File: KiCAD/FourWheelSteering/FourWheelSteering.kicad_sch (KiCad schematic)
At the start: 11 parts, among them J1 Conn_01x04_Pin, U1 Q1, U2 Q3, U3 Q2, U4 Q4

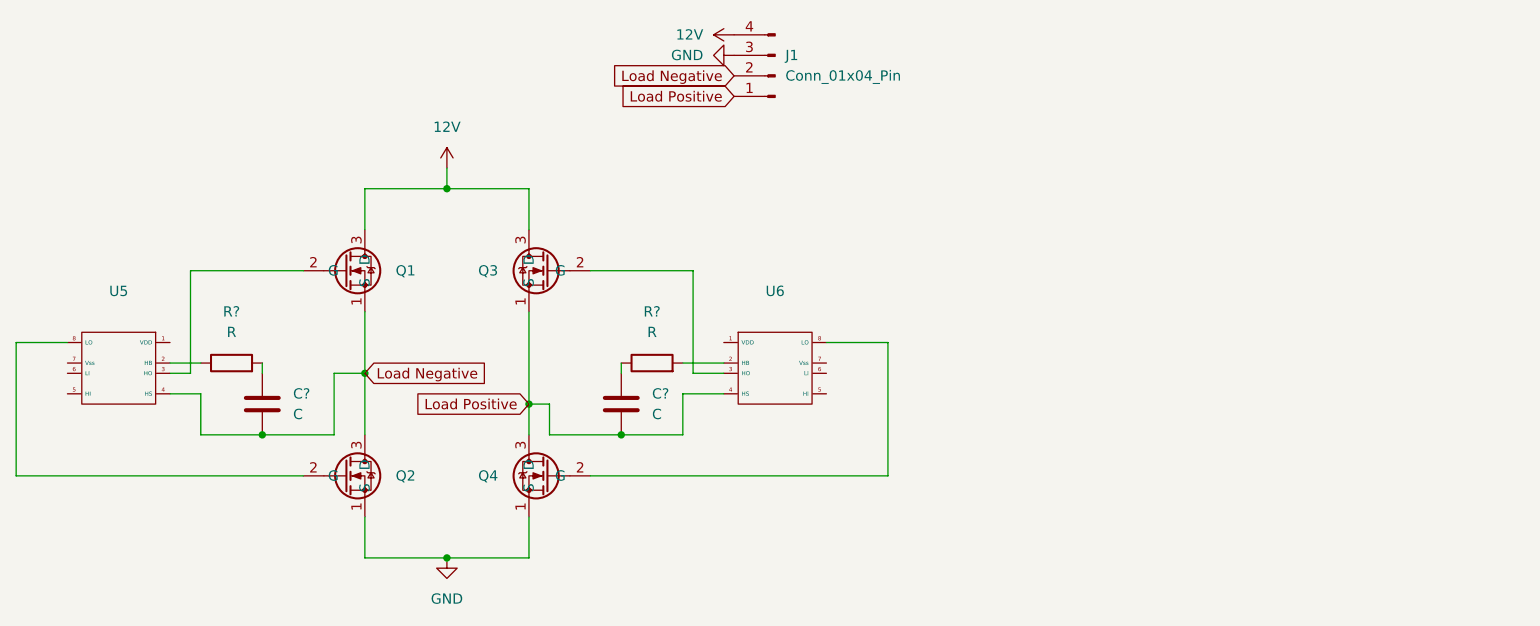
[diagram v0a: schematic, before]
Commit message: Updated KiCAD symbols and footprints for MSPM1306
SDFAGD
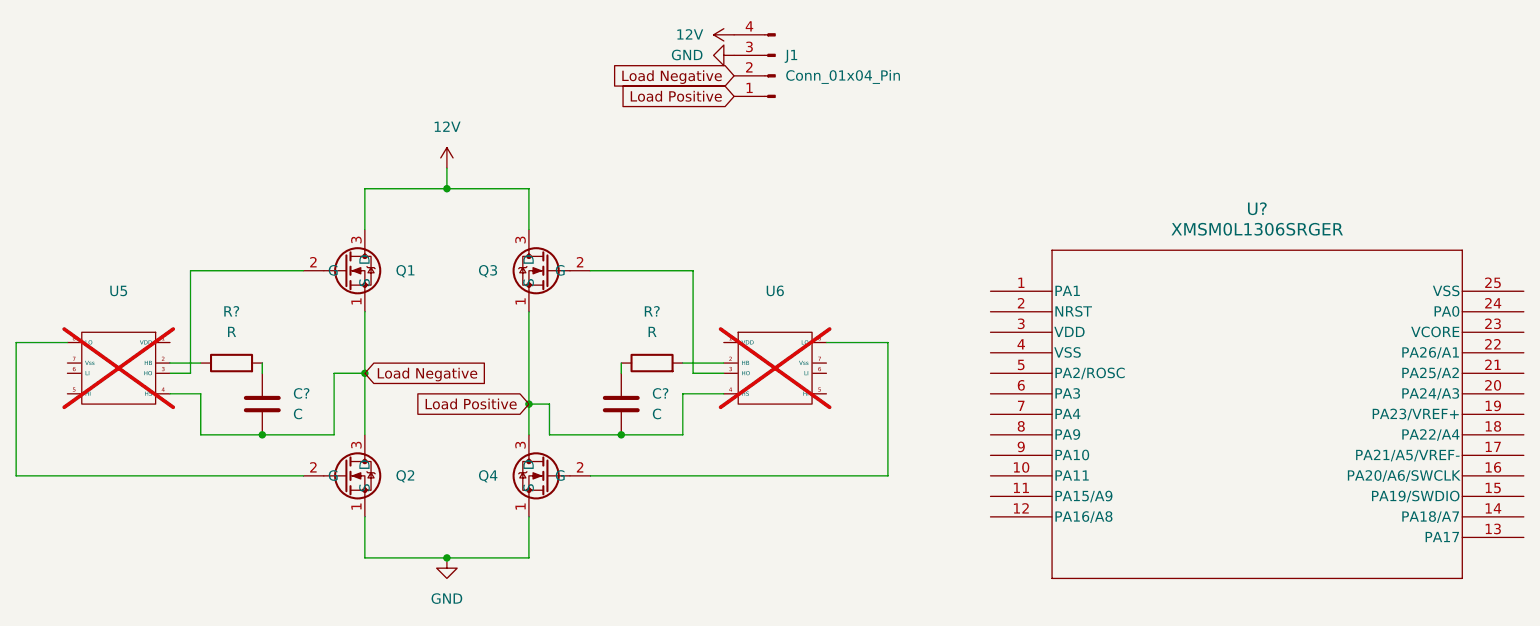
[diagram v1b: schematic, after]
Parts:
- added U?: XMSM0L1306SRGER, Library:VQFN24_RGE_TEX, symbol FWSLibrary:XMSM0L1306SRGER
- U5, U6: now not fitted; now left out of the parts list
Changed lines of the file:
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@@
 		(mirror y)
 		(unit 1)
-		(exclude_from_sim no)
-		(in_bom yes)
-		(on_board yes)
-		(dnp no)
+		(exclude_from_sim yes)
+		(in_bom no)
+		(on_board no)
+		(dnp yes)
 		(fields_autoplaced yes)
 		(property "Reference" "U5"
@@
 	)
 	(symbol
+		(lib_id "FWSLibrary:XMSM0L1306SRGER")
+		(at 186.69 91.44 0)
+		(unit 1)
+		(exclude_from_sim no)
+		(in_bom yes)
+		(on_board yes)
+		(dnp no)
+		(fields_autoplaced yes)
+		(property "Reference" "U?"
+			(at 219.71 81.28 0)
+			(effects
+				(font
+					(size 1.524 1.524)
+				)
+			)
+		)
+		(property "Value" "XMSM0L1306SRGER"
+			(at 219.71 83.82 0)
+			(effects
+				(font
+					(size 1.524 1.524)
+				)
+			)
+		)
+		(property "Footprint" "Library:VQFN24_RGE_TEX"
+			(at 186.69 91.44 0)
+			(effects
+				(font
+					(size 1.27 1.27)
+					(italic yes)
+				)
+				(hide yes)
+			)
+		)
+		(property "Datasheet" "https://www.ti.com/lit/gpn/mspm0l1306"
+			(at 186.69 91.44 0)
+			(effects
+				(font
+					(size 1.27 1.27)
+					(italic yes)
+				)
+				(hide yes)
+			)
+		)
+		(property "Description" ""
+			(at 186.69 91.44 0)
+			(effects
+				(font
+					(size 1.27 1.27)
+				)
+				(hide yes)
+			)
+		)
+		(pin "2"
+		)
+		(pin "25"
+		)
+		(pin "7"
+		)
+		(pin "12"
+		)
+		(pin "3"
+		)
+		(pin "1"
+		)
+		(pin "5"
+		)
+		(pin "9"
+		)
+		(pin "10"
+		)
+		(pin "6"
+		)
+		(pin "8"
+		)
+		(pin "11"
+		)
+		(pin "13"
+		)
+		(pin "4"
+		)
+		(pin "24"
+		)
+		(pin "23"
+		)
+		(pin "20"
+		)
+		(pin "18"
+		)
+		(pin "22"
+		)
+		(pin "21"
+		)
+		(pin "19"
+		)
+		(pin "17"
+		)
+		(pin "16"
+		)
+		(pin "15"
+		)
+		(pin "14"
+		)
+		(instances
+			(project ""
+				(path "/991cfcb0-d7e9-4e4d-a675-64d82c95fcae"
+					(reference "U?")
+					(unit 1)
+				)
+			)
+		)
+	)
+	(symbol
 		(lib_id "Device:C")
 		(at 96.52 105.41 0)
@@
 		(at 154.94 106.68 0)
 		(unit 1)
-		(exclude_from_sim no)
-		(in_bom yes)
-		(on_board yes)
-		(dnp no)
+		(exclude_from_sim yes)
+		(in_bom no)
+		(on_board no)
+		(dnp yes)
 		(fields_autoplaced yes)
 		(property "Reference" "U6"
